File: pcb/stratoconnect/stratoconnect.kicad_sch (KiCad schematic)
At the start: 48 parts, among them J1 Conn_Coaxial, J2 Conn_02x03_Odd_Even, J3 Conn_01x05_Male, J4 Conn_01x02_Male, J5 Conn_01x03_Male, SW1 SW_SPST, SW2 SW_SPST, U1 RF4463f30, U2 ATmega328PB-A, U3 TPS61022RWU, U4 PCA9306DC, Y1 CSTNE16M0V530000R0

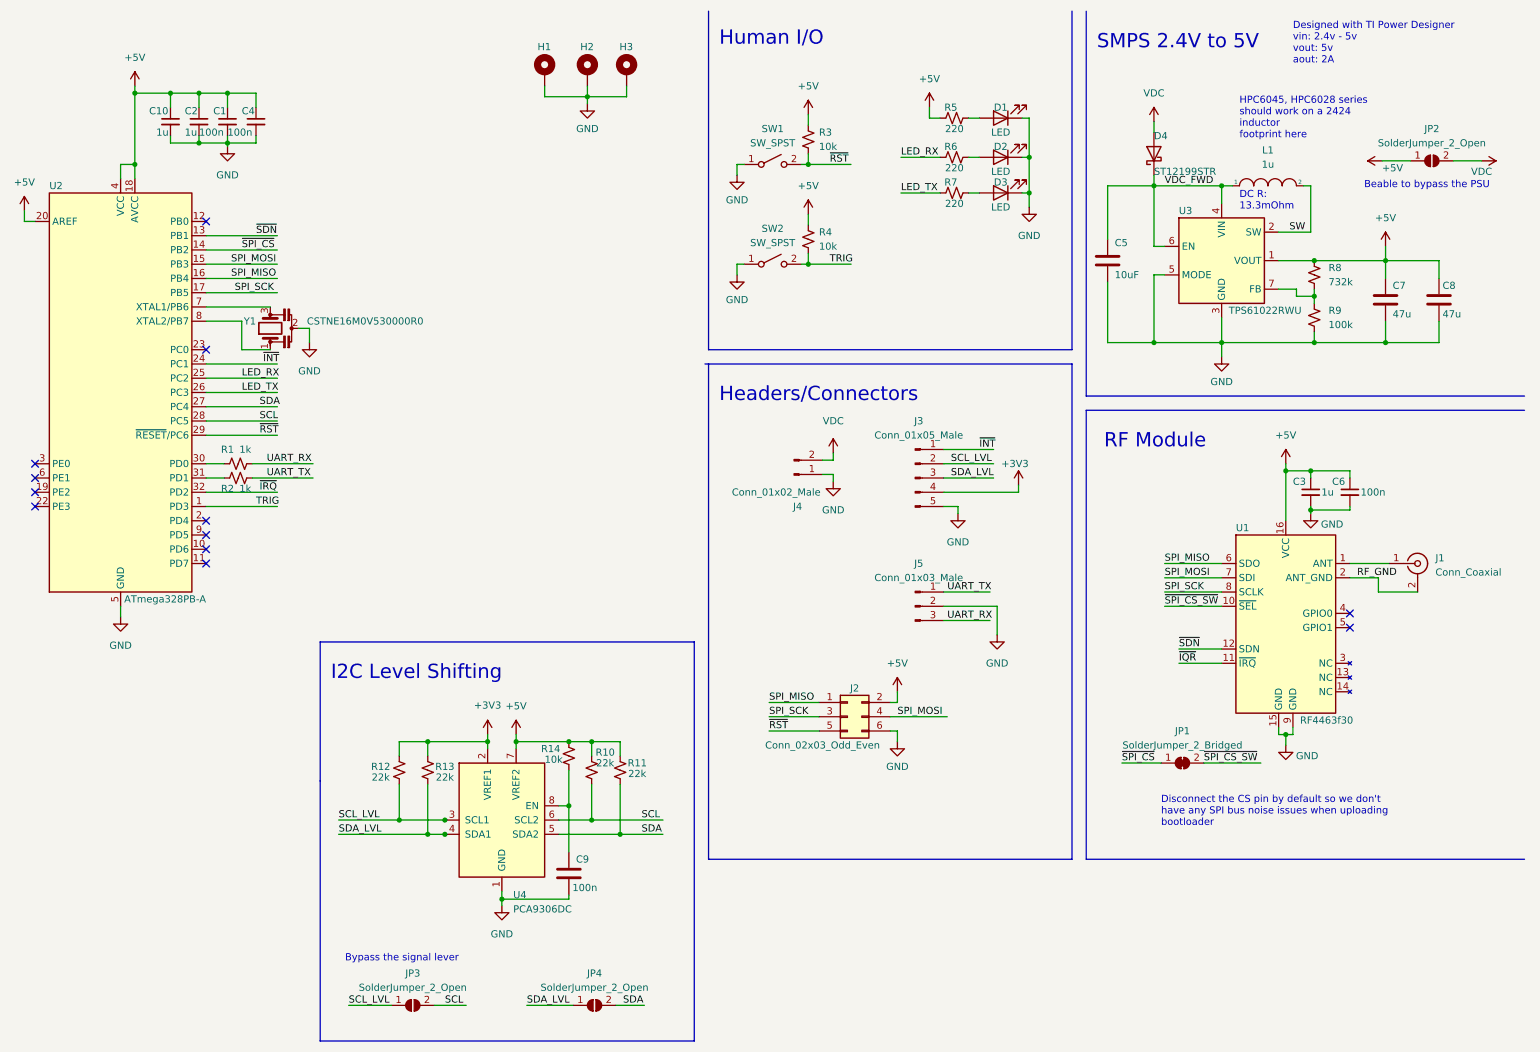
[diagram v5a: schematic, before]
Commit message: add labels update rf lib
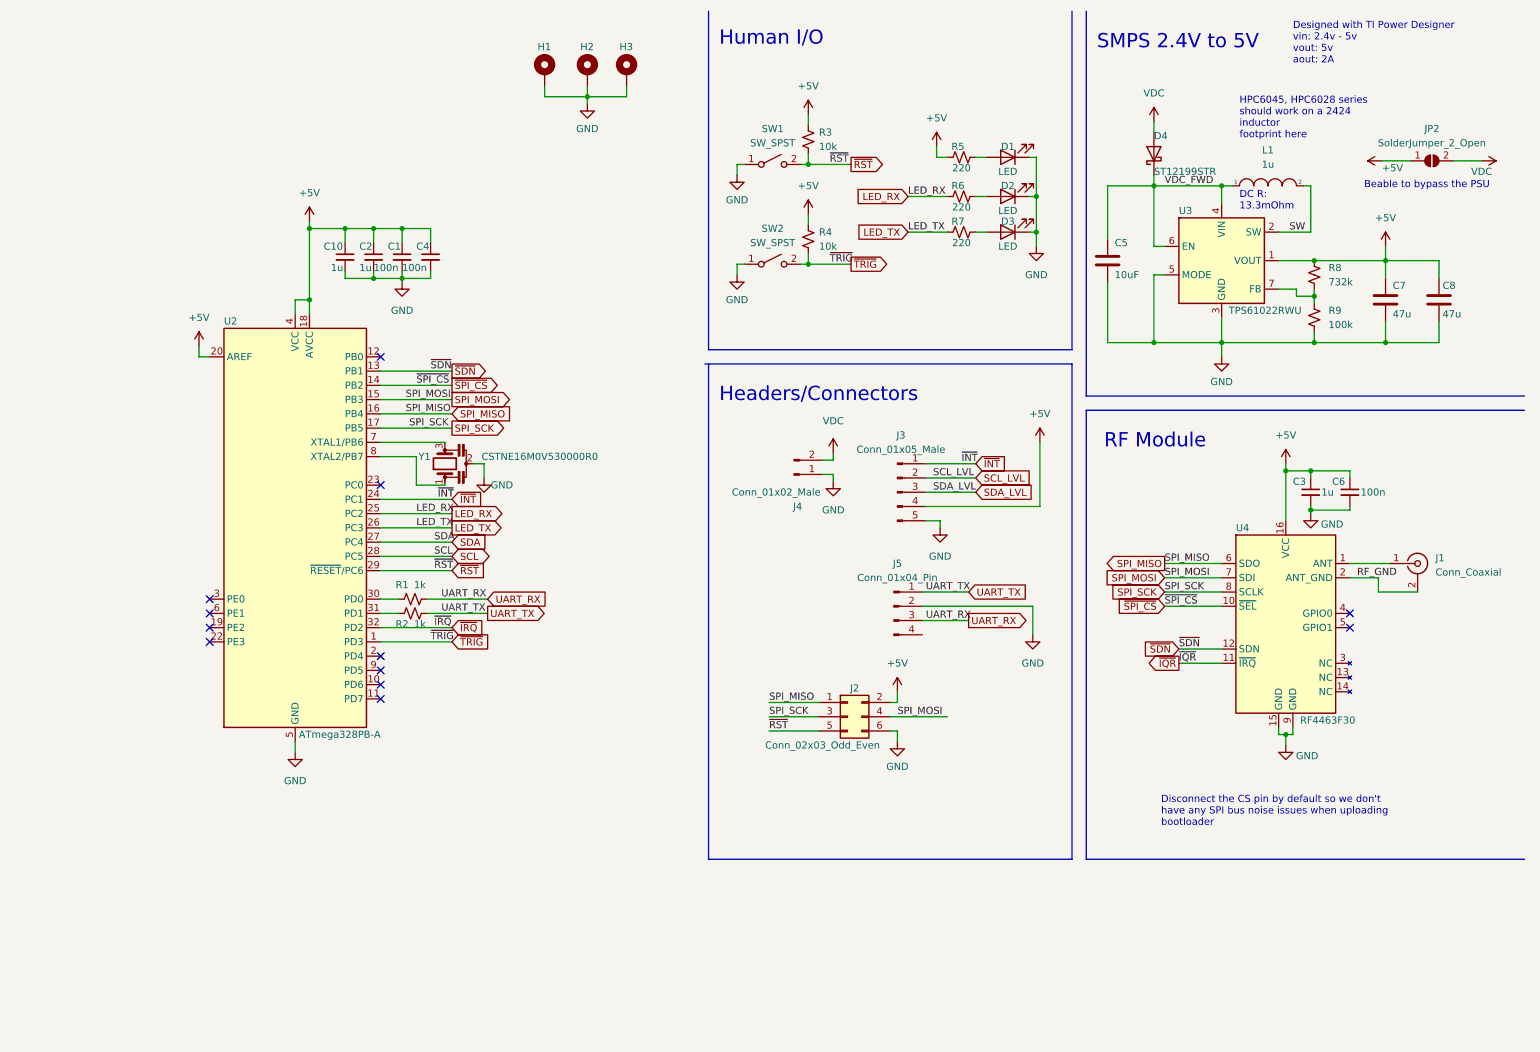
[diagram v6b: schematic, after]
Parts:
- removed C9: 100n, Capacitor_SMD:C_0603_1608Metric, symbol Device:C
- removed J5: Conn_01x03_Male, Connector_JST:JST_GH_SM03B-GHS-TB_1x03-1MP_P1.25mm_Horizontal, symbol Connector:Conn_01x03_Male
- removed JP1: SolderJumper_2_Bridged, Jumper:SolderJumper-2_P1.3mm_Bridged_RoundedPad1.0x1.5mm, symbol Jumper:SolderJumper_2_Bridged
- removed JP3, JP4: SolderJumper_2_Open, Jumper:SolderJumper-2_P1.3mm_Open_RoundedPad1.0x1.5mm, symbol Jumper:SolderJumper_2_Open
- removed R10, R11, R12, R13: 22k, Resistor_SMD:R_0603_1608Metric, symbol Device:R_Small_US
- removed R14: 10k, Resistor_SMD:R_0603_1608Metric, symbol Device:R_Small_US
- removed U1: RF4463f30, RF:RF4463F30, symbol RF_Module:RF4463f30
- removed U4: PCA9306DC, Package_SO:VSSOP-8_2.3x2mm_P0.5mm, symbol Interface:PCA9306DC
- added J5: Conn_01x04_Pin, symbol Connector:Conn_01x04_Pin
- added U4: RF4463F30, Kevin_Lutzer_Lbr:RF4463F30, symbol Kevin_Lutzer_Lbr:RF4463f30
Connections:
- net +3V3 is gone; now on net +5V: J3.4 (Pin_4)
- net +5V: now also U4.16 (VCC)
- net GND: now also J5.2 (Pin_2), U4.15 (GND), U4.9 (GND)
- net RF_GND: now also U4.2 (ANT_GND)
- net SPI_MISO: now also U4.6 (SDO)
- net SPI_MOSI: now also U4.7 (SDI)
- net SPI_SCK: now also U4.8 (SCLK)
- net UART_RX: now also J5.3 (Pin_3)
- net UART_TX: now also J5.1 (Pin_1)
- net ~{IQR}: now also U4.11 (~{IRQ})
- net ~{SDN}: now also U4.12 (SDN)
- net ~{SPI_CS}: now also U4.10 (~{SEL})
- net at J1.1 (In): now also U4.1 (ANT)
- net TRIG renamed ~{TRIG}
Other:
- note removed: "Bypass the signal lever"
- note removed: "I2C Level Shifting"
- moved on the sheet: C1, C10, C2, C4, D1, D2, D3, J3, R1, R2, R5, R6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

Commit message: remove the i2c level shifter, add the TPS565 smps chip
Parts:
- removed U3: TPS61022RWU, Package_DFN_QFN:VDFN-7_2.1x2.1mm, symbol Regulator_Switching:TPS61022RWU
- added C11: 33p, Capacitor_SMD:CP_Elec_5x5.3, symbol Device:C
- added C9: 100n, Capacitor_SMD:CP_Elec_5x5.3, symbol Device:C
- added R10: 100k, Resistor_SMD:R_0805_2012Metric, symbol Device:R_Small_US
- added R11: 25.5k, Resistor_SMD:R_0805_2012Metric, symbol Device:R_Small_US
- added U1: TPS565242, Package_TO_SOT_SMD:SOT-563, symbol Kevin_Lutzer_Lbr:TPS565242
- L1: value 1u -> 3.3u
- R8: value 732k -> 158k
- R9: value 100k -> 30k
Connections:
- net +5V: now also L1.2, C11.1
- net GND: now also R11.2, U1.1 (GND)
- net SW: now also L1.1, C9.1, U1.2 (SW); no longer L1.2
- net FB: now reaches R8.2, R9.1
- net FB: now also C11.2, U1.4 (VFB)
- net VDC_FWD: no longer names the net of C5.1, D4.1 (K)
- net VDC_FWD: now also R10.1, U1.3 (VIN); no longer L1.1
- new net: C9.2, U1.6 (VBST)
- new net EN: R10.2, R11.1, U1.5 (EN)
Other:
- note added: "DC R: 40mOhm"
- note added: "Designed with TI Power Designer vin: 6v - 9v vout: 5v aout: 2A"
- note added: "Keep C9 and C11 With a Low DC Like 1m"
- note added: "Max 6 volts on the EN pin So lets use a voltage divider here"
- note added: "SMPS 6V to 9V"
- note removed: "DC R: 13.3mOhm"
- note removed: "Designed with TI Power Designer vin: 2.4v - 5v vout: 5v aout: 2A"
- note removed: "HPC6045, HPC6028 series should work on a 2424 inductor footprint here"
- note removed: "SMPS 2.4V to 5V"
- moved on the sheet: C5, C7, C8, D1, D2, D3, D4, J2, J3, J4, J5, JP2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

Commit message: fix all the  erc warnings
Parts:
- removed J3: Conn_01x05_Male, Connector_JST:JST_GH_SM05B-GHS-TB_1x05-1MP_P1.25mm_Horizontal, symbol Connector:Conn_01x05_Male
- removed J4: Conn_01x02_Male, Connector_JST:JST_EH_S2B-EH_1x02_P2.50mm_Horizontal, symbol Connector:Conn_01x02_Male
- removed J5: Conn_01x04_Pin, symbol Connector:Conn_01x04_Pin
- removed L1: 3.3u, Inductor_SMD:L_2440_6060Metric, symbol pspice:INDUCTOR
- added J3: Conn_01x04_Pin, symbol Connector:Conn_01x04_Pin
- added J4: Conn_01x02_Pin, symbol Connector:Conn_01x02_Pin
- added J5: Conn_01x05_Pin, symbol Connector:Conn_01x05_Pin
- added L1: L, Inductor_SMD_Wurth:L_Wurth_WE-LQSH-4020, symbol Device:L
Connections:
- net ~{IQR} is gone; now on net ~{IRQ}: U4.11 (~{IRQ})
- net +5V: now also J5.4 (Pin_4), L1.2
- net GND: now also J3.2 (Pin_2), J4.2 (Pin_2), J5.5 (Pin_5)
- net SCL: now also J5.2 (Pin_2)
- net SDA: now also J5.3 (Pin_3)
- net SW: now also L1.1
- net UART_RX: now also J3.3 (Pin_3)
- net UART_TX: now also J3.1 (Pin_1)
- net VDC: now also J4.1 (Pin_1)
- net ~{INT}: now also J5.1 (Pin_1)
- net ~{RST}: now also J3.4 (Pin_4)
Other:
- moved on the sheet: C1, C10, C11, C2, C4, C7, C8, D1, D2, D3, H1, H2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
